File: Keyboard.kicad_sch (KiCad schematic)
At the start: 33 parts, among them J1 USB_mini_micro_B, SW1 SW_PUSH, SW1 SW_Push, U1 ATMEGA32U4, U2 ATmega32U4-A, X1 XTAL_GND, Y1 16MHz

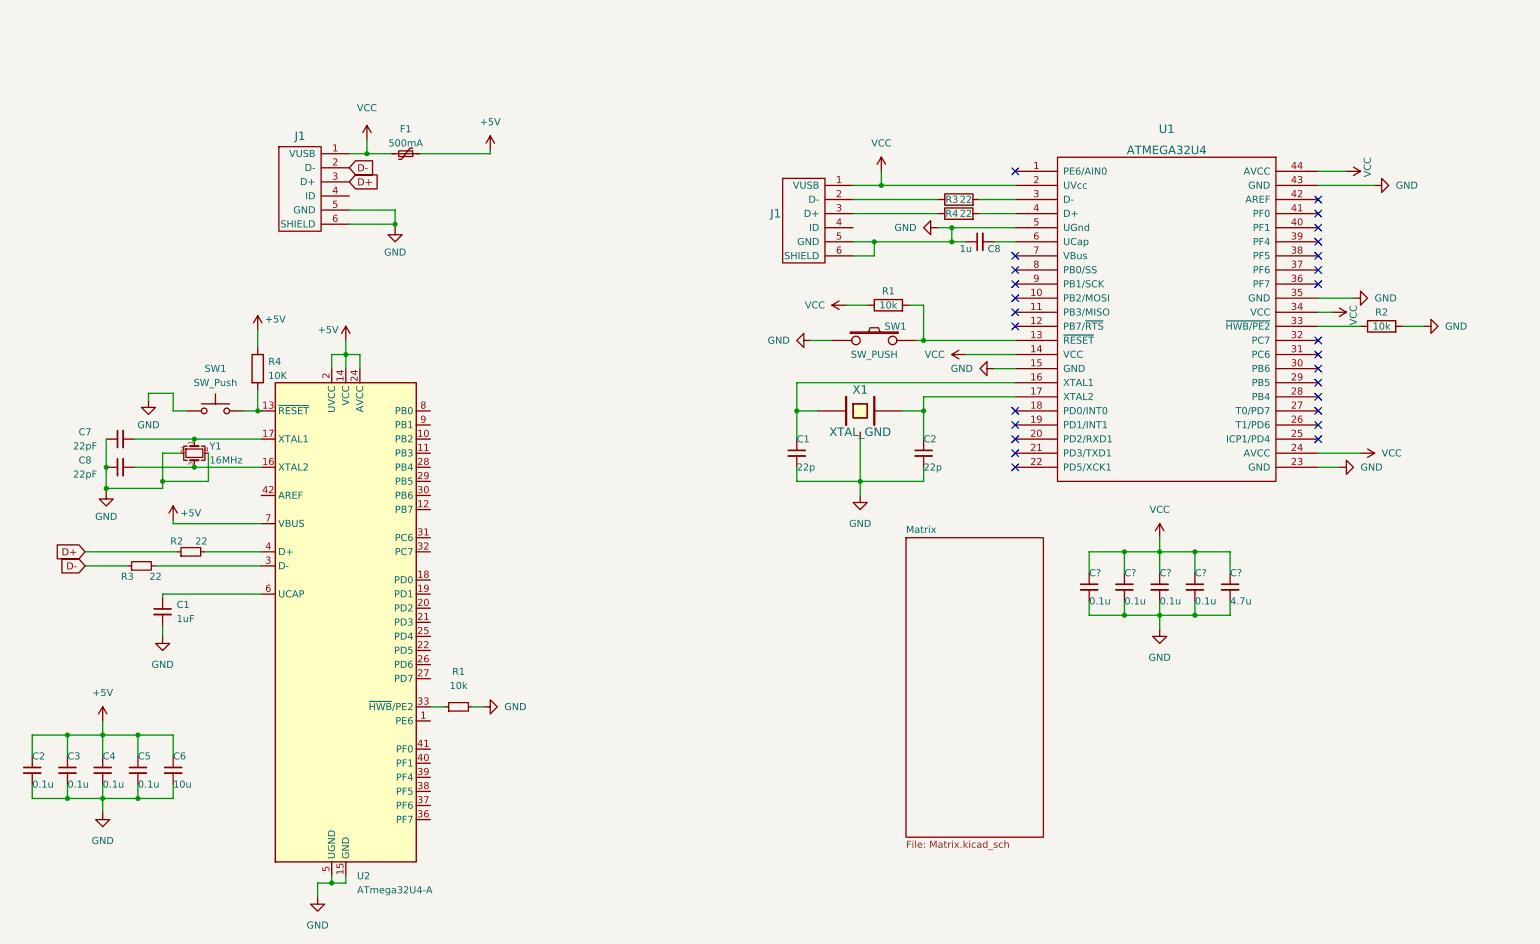
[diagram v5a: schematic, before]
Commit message: Connected some columns to MCU and cleaned up main schema
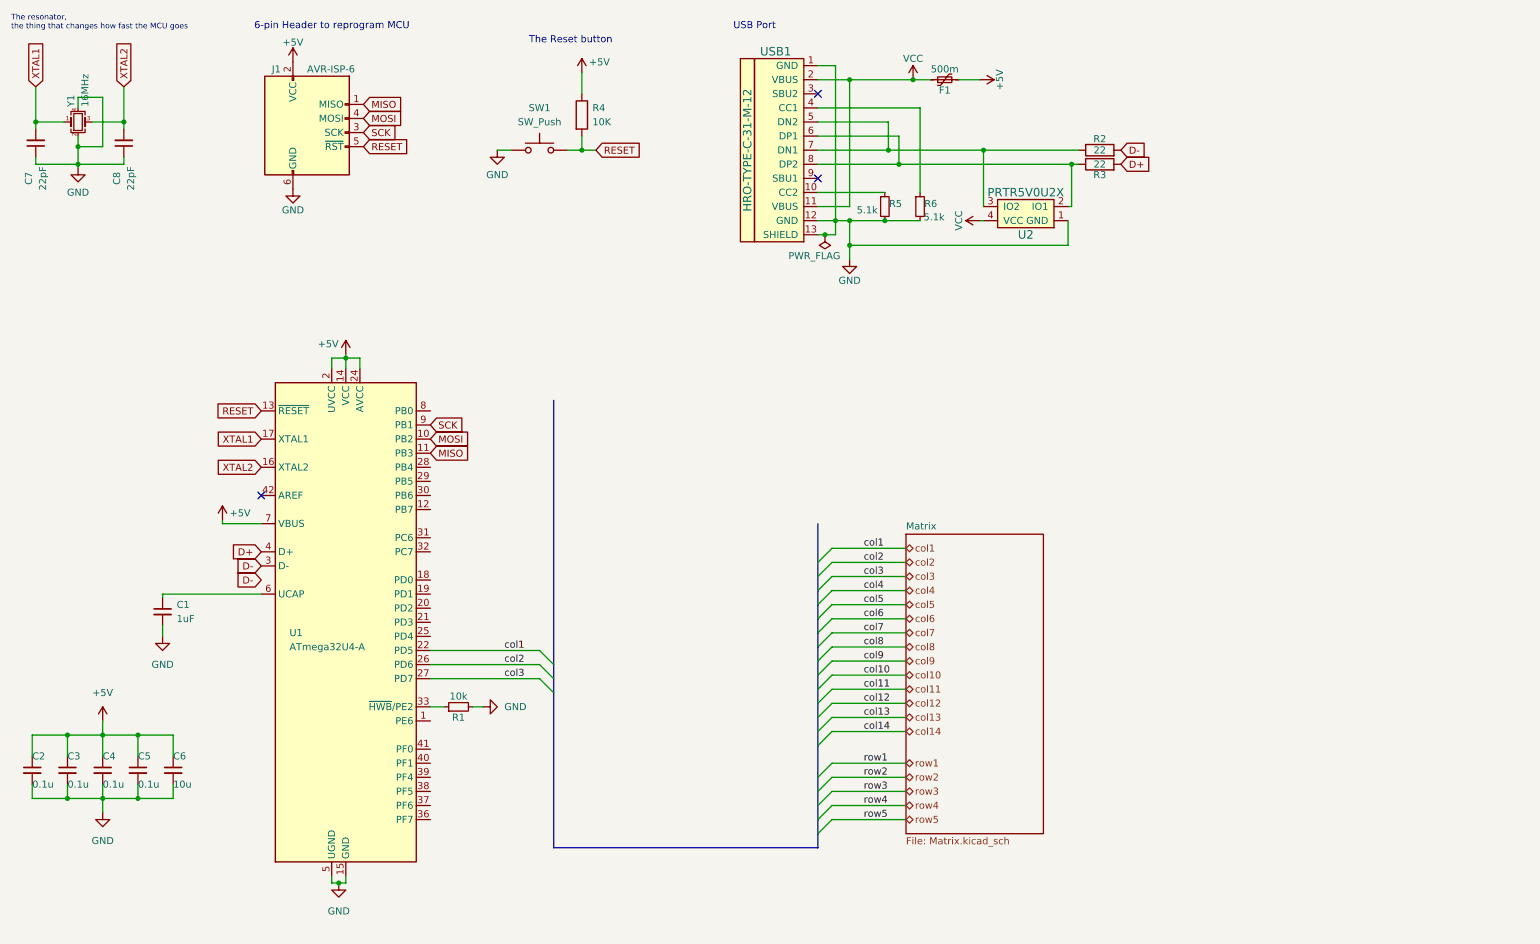
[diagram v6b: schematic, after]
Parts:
- removed C1, C2: 22p, symbol Device:C_Small
- removed C8: 1u, symbol Device:C_Small
- removed C? (x4): 0.1u, symbol Device:C_Small
- removed C?: 4.7u, symbol Device:C_Small
- removed J1 (x2): USB_mini_micro_B, symbol keyboard_parts:USB_mini_micro_B
- removed R1: 10k, symbol Device:R
- removed R2, R3: 22, symbol Device:R_Small
- removed R4: 22, symbol Device:R
- removed SW1: SW_PUSH, symbol keyboard_parts:SW_PUSH
- removed U1: ATMEGA32U4, symbol keyboard_parts:ATMEGA32U4
- removed X1: XTAL_GND, symbol keyboard_parts:XTAL_GND
- added J1: AVR-ISP-6, symbol Connector:AVR-ISP-6
- added R5, R6: 5.1k, symbol Device:R_Small
- added U2: PRTR5V0U2X, symbol random-keyboard-parts:PRTR5V0U2X
- added USB1: HRO-TYPE-C-31-M-12, symbol Type-C:HRO-TYPE-C-31-M-12
- F1: value 500mA -> 500m
- R2: value 10k -> 22
- renumbered U2 to U1
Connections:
- net +5V: now also J1.2 (VCC)
- net D+: now also R3.2, U1.4 (D+)
- net D-: now also R2.2, U1.3 (D-)
- net GND: now also J1.6 (GND), R5.2, R6.2, U2.1 (GND), USB1.1 (GND), USB1.12 (GND), USB1.13 (SHIELD); no longer R2.2
- net VCC: now also U2.4 (VCC), USB1.11 (VBUS), USB1.2 (VBUS)
- net XTAL1: now reaches C7.2, U1.17 (XTAL1), Y1.1
- net at R3.1: now also U2.2 (IO1), USB1.6 (DP1), USB1.8 (DP2)
- net XTAL2: now reaches C8.2, U1.16 (XTAL2), Y1.3
- net RESET: now reaches R4.2, SW1.2, U1.13 (~{RESET})
- net RESET: now also J1.5 (~{RST})
- net MOSI: now reaches U1.10 (PB2)
- net MOSI: now also J1.4 (MOSI)
- net MISO: now reaches U1.11 (PB3)
- net MISO: now also J1.1 (MISO)
- net col1: now reaches U1.22 (PD5)
- net col2: now reaches U1.26 (PD6)
- net col3: now reaches U1.27 (PD7)
- net SCK: now reaches U1.9 (PB1)
- net SCK: now also J1.3 (SCK)
- net at R2.1: now also U2.3 (IO2), USB1.5 (DN2), USB1.7 (DN1)
- new net: R5.1, USB1.10 (CC2)
- new net: R6.1, USB1.4 (CC1)
- no-connect marks 27 -> 3
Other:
- note added: "6-pin Header to reprogram MCU"
- note added: "The Reset button"
- note added: "The resonator, the thing that changes how fast the MCU goes"
- note added: "USB Port"
- moved on the sheet: C7, C8, R4, SW1, Y1

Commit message: Assigned footprints and connected all rows and columns to MCU
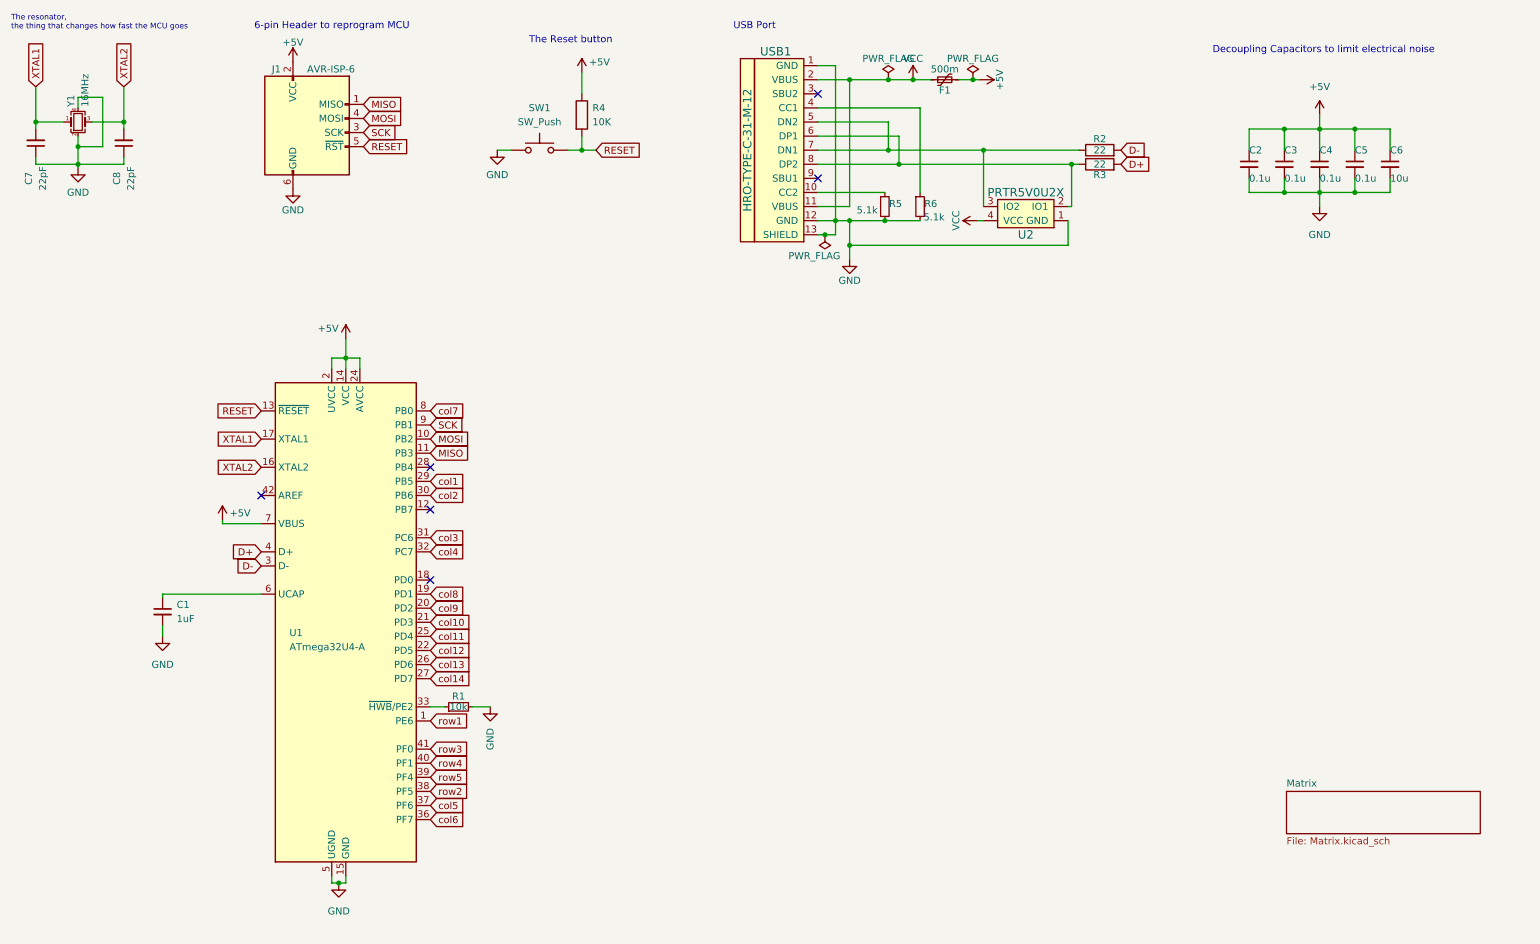
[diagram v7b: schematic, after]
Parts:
- C1, C2, C3, C4, C5, C6, C7, C8: footprint (none) -> Capacitor_SMD:C_0805_2012Metric_Pad1.18x1.45mm_HandSolder
- F1: footprint (none) -> Fuse:Fuse_1206_3216Metric_Pad1.42x1.75mm_HandSolder
- J1: footprint (none) -> random-keyboard-parts:Reset_Pretty-Mask
- R1, R2, R3, R4, R5, R6: footprint (none) -> Resistor_SMD:R_0805_2012Metric_Pad1.20x1.40mm_HandSolder
- SW1: footprint (none) -> Button_Switch_SMD:SW_SPST_SKQG_WithStem
- U2: footprint (none) -> random-keyboard-parts:SOT143B
- USB1: footprint (none) -> Type-C:HRO-TYPE-C-31-M-12-HandSoldering
- Y1: footprint (none) -> Crystal:Crystal_SMD_3225-4Pin_3.2x2.5mm_HandSoldering
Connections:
- net col1: now also U1.29 (PB5); no longer U1.22 (PD5)
- net col10: now also U1.21 (PD3)
- net col11: now also U1.25 (PD4)
- net col12: now also U1.22 (PD5)
- net col13: now also U1.26 (PD6)
- net col14: now also U1.27 (PD7)
- net col2: now also U1.30 (PB6); no longer U1.26 (PD6)
- net col3: now also U1.31 (PC6); no longer U1.27 (PD7)
- net col4: now also U1.32 (PC7)
- net col5: now also U1.37 (PF6)
- net col6: now also U1.36 (PF7)
- net col7: now also U1.8 (PB0)
- net col8: now also U1.19 (PD1)
- net col9: now also U1.20 (PD2)
- net row1: now also U1.1 (PE6)
- net row2: now also U1.38 (PF5)
- net row3: now also U1.41 (PF0)
- net row4: now also U1.40 (PF1)
- net row5: now also U1.39 (PF4)
- no-connect marks 3 -> 6
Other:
- note added: "Decoupling Capacitors to limit electrical noise"
- moved on the sheet: C2, C3, C4, C5, C6

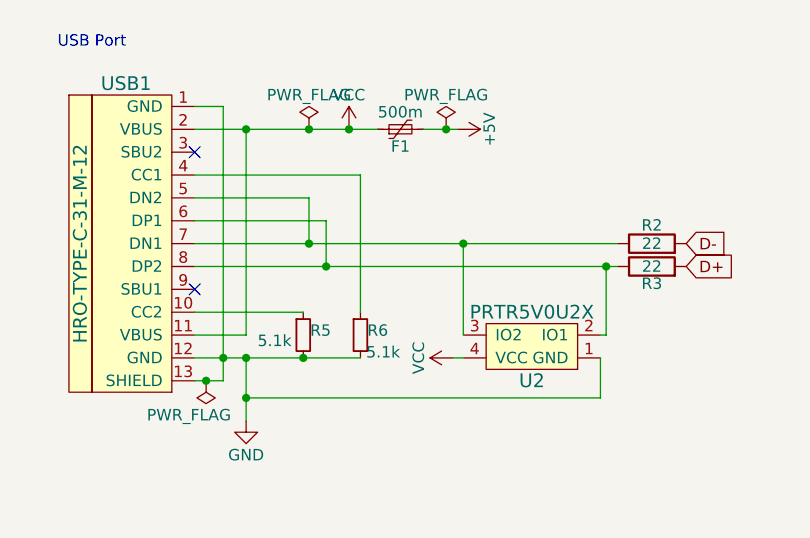
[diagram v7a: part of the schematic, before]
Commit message: Connected D- and D+ on MCU to both D- and both D+ on Type-C connector
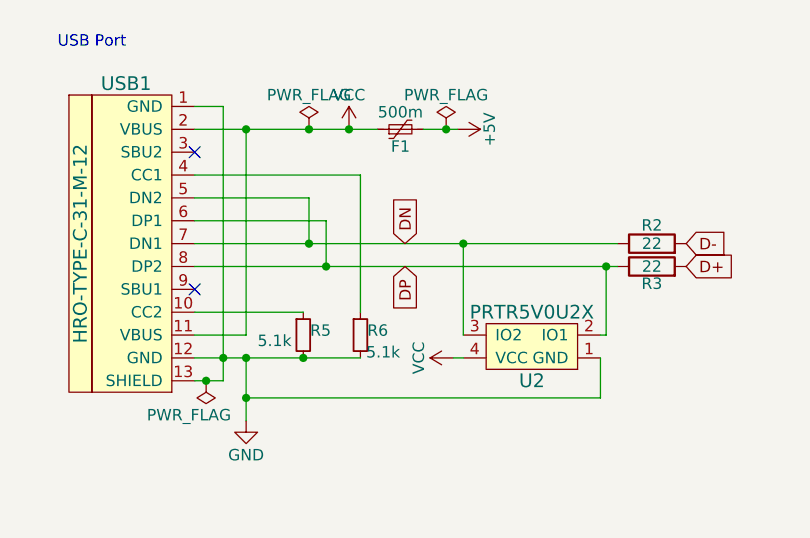
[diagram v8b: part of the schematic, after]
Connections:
- net DN: now reaches R2.1, U2.3 (IO2), USB1.5 (DN2), USB1.7 (DN1)
- net DP: now reaches R3.1, U2.2 (IO1), USB1.6 (DP1), USB1.8 (DP2)
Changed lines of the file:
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@@
+    )
+  )
+  (global_label "DN" (shape input) (at 183.388 39.37 90) (fields_autoplaced)
+    (effects (font (size 1.27 1.27)) (justify left))
+    (property "Intersheet References" "${INTERSHEET_REFS}" (id 0) (at 183.3086 34.3564 90)
+      (effects (font (size 1.27 1.27)) (justify left) hide)
     )
   )
@@
     )
   )
+  (global_label "DP" (shape input) (at 183.388 41.91 270) (fields_autoplaced)
+    (effects (font (size 1.27 1.27)) (justify right))
+    (property "Intersheet References" "${INTERSHEET_REFS}" (id 0) (at 183.3086 46.8631 90)
+      (effects (font (size 1.27 1.27)) (justify right) hide)
+    )
+  )
